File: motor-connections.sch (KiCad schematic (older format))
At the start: 21 parts, among them J3 Conn_02x01, J4 Motor, J5 Rotary_Encoder, Q1 Q_NPN_BEC, Q2 SiSS05DN, U3 OPA333xxDCK

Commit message: First draft of a pcb layout
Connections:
- net +3V3: now also J5.1 (Pin_1)
- net +8V: no longer J5.1 (Pin_1)

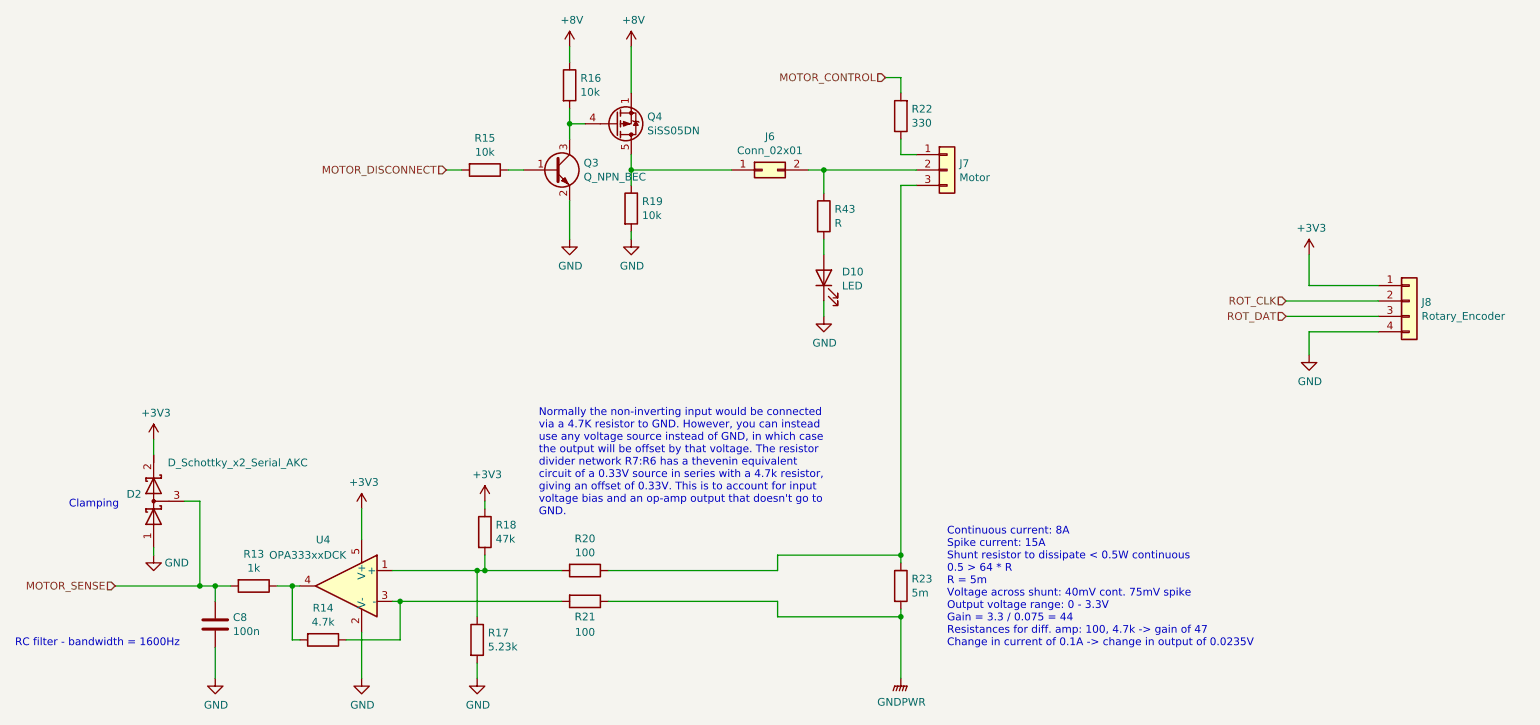
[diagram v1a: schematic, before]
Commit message: Placed components on the PCB
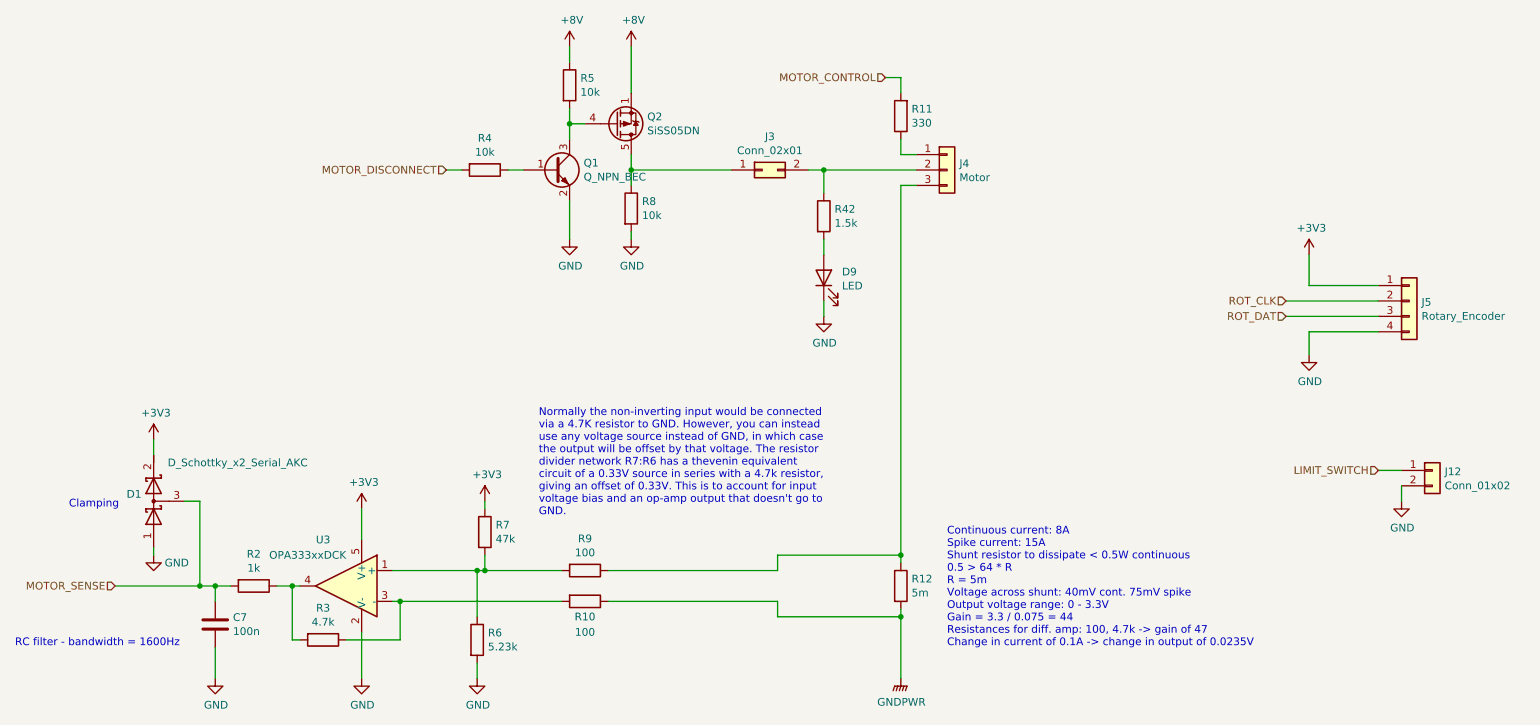
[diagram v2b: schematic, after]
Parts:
- added J12: Conn_01x02, Connector_PinHeader_2.54mm:PinHeader_1x02_P2.54mm_Vertical, symbol Connector_Generic:Conn_01x02
- R10, R11, R2, R3, R4, R5, R6, R7, R8, R9: footprint Resistor_SMD:R_0603_1608Metric_Pad1.05x0.95mm_HandSolder -> Resistor_SMD:R_0603_1608Metric
- R43: value R -> 1.5k; footprint Resistor_SMD:R_0603_1608Metric_Pad1.05x0.95mm_HandSolder -> Resistor_SMD:R_0603_1608Metric
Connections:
- net GND: now also J12.2 (Pin_2)
- new net LIMIT_SWITCH: J12.1 (Pin_1)
